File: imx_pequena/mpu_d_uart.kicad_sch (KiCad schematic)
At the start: 1 part, among them U1 MCIMX6Z0DVM09AB

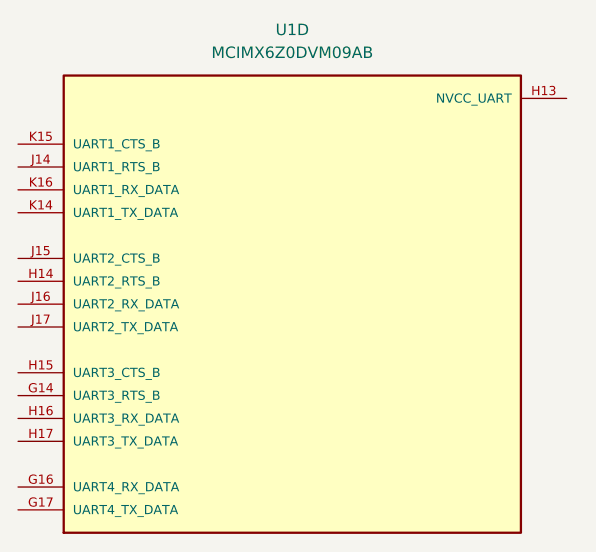
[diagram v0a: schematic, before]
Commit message: SD card + pinot files
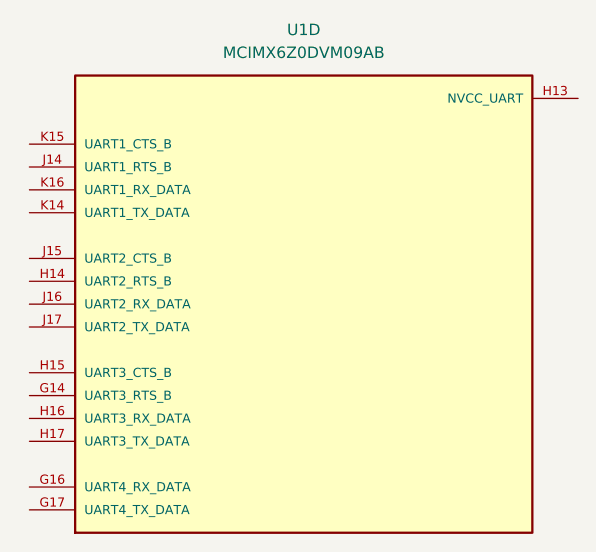
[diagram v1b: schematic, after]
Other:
- moved on the sheet: U1D
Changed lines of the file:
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@@
 (kicad_sch (version 20211123) (generator eeschema)
   (paper "A4")
-  (symbol (lib_id "MCIMX6Z0DVM09AB:MCIMX6Z0DVM09AB") (at 132.08 76.2 0) (unit 4)
+  (symbol (lib_id "MCIMX6Z0DVM09AB:MCIMX6Z0DVM09AB") (at 133.35 76.2 0) (unit 4)
     (in_bom yes) (on_board yes) (fields_autoplaced)
-    (property "Reference" "U1" (id 0) (at 132.08 45.72 0))
-    (property "Value" "MCIMX6Z0DVM09AB" (id 1) (at 132.08 48.26 0))
-    (property "Footprint" "mb_nxp_mcu_mpu:BGA289C80P17X17_1400X1400X132" (id 2) (at 132.08 76.2 0)
+    (property "Reference" "U1" (id 0) (at 133.35 45.72 0))
+    (property "Value" "MCIMX6Z0DVM09AB" (id 1) (at 133.35 48.26 0))
+    (property "Footprint" "mb_nxp_mcu_mpu:BGA289C80P17X17_1400X1400X132" (id 2) (at 133.35 76.2 0)
       (effects (font (size 1.27 1.27)) (justify bottom) hide)
     )
-    (property "Datasheet" "" (id 3) (at 132.08 76.2 0)
+    (property "Datasheet" "" (id 3) (at 133.35 76.2 0)
       (effects (font (size 1.27 1.27)) hide)
     )
-    (property "PARTREV" "0" (id 4) (at 132.08 76.2 0)
+    (property "PARTREV" "0" (id 4) (at 133.35 76.2 0)
       (effects (font (size 1.27 1.27)) (justify bottom) hide)
     )
-    (property "STANDARD" "IPC 7351B" (id 5) (at 132.08 76.2 0)
+    (property "STANDARD" "IPC 7351B" (id 5) (at 133.35 76.2 0)
       (effects (font (size 1.27 1.27)) (justify bottom) hide)
     )
-    (property "SNAPEDA_PN" "MCIMX6Z0DVM09AB" (id 6) (at 132.08 76.2 0)
+    (property "SNAPEDA_PN" "MCIMX6Z0DVM09AB" (id 6) (at 133.35 76.2 0)
       (effects (font (size 1.27 1.27)) (justify bottom) hide)
     )
-    (property "MAXIMUM_PACKAGE_HEIGHT" "1.32mm" (id 7) (at 132.08 76.2 0)
+    (property "MAXIMUM_PACKAGE_HEIGHT" "1.32mm" (id 7) (at 133.35 76.2 0)
       (effects (font (size 1.27 1.27)) (justify bottom) hide)
     )
-    (property "MANUFACTURER" "NXP" (id 8) (at 132.08 76.2 0)
+    (property "MANUFACTURER" "NXP" (id 8) (at 133.35 76.2 0)
       (effects (font (size 1.27 1.27)) (justify bottom) hide)
     )

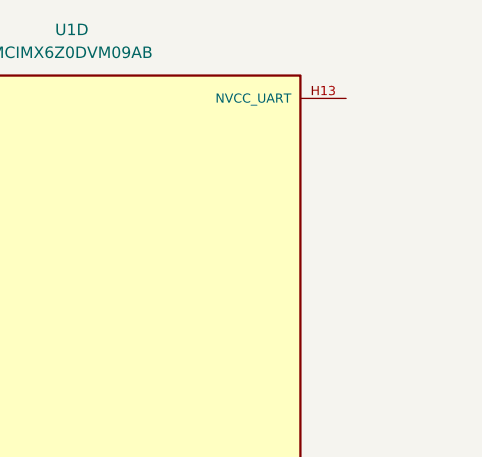
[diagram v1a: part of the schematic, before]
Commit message: Power Update
Added 3v3 and 1.35V switchers
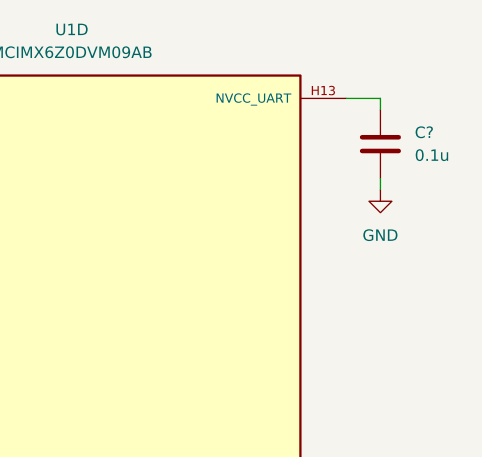
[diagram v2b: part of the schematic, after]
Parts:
- added C?: 0.1u, symbol Device:C
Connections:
- net at U1.H13 (NVCC_UART): now also C?.1
- new net GND: C?.2
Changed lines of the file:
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@@
 (kicad_sch (version 20211123) (generator eeschema)
   (paper "A4")
+  (wire (pts (xy 167.64 53.34) (xy 167.64 54.61))
+    (stroke (width 0) (type default) (color 0 0 0 0))
+  )
+  (wire (pts (xy 163.83 53.34) (xy 167.64 53.34))
+    (stroke (width 0) (type default) (color 0 0 0 0))
+  )
+  (wire (pts (xy 167.64 62.23) (xy 167.64 63.5))
+    (stroke (width 0) (type default) (color 0 0 0 0))
+  )
+  (symbol (lib_id "Device:C") (at 167.64 58.42 0) (unit 1)
+    (in_bom yes) (on_board yes) (fields_autoplaced)
+    (property "Reference" "C?" (id 0) (at 171.45 57.1499 0)
+      (effects (font (size 1.27 1.27)) (justify left))
+    )
+    (property "Value" "0.1u" (id 1) (at 171.45 59.6899 0)
+      (effects (font (size 1.27 1.27)) (justify left))
+    )
+    (property "Footprint" "" (id 2) (at 168.6052 62.23 0)
+      (effects (font (size 1.27 1.27)) hide)
+    )
+    (property "Datasheet" "~" (id 3) (at 167.64 58.42 0)
+      (effects (font (size 1.27 1.27)) hide)
+    )
+    (pin "1")
+    (pin "2")
+  )
+  (symbol (lib_id "power:GND") (at 167.64 63.5 0) (unit 1)
+    (in_bom yes) (on_board yes) (fields_autoplaced)
+    (property "Reference" "#PWR?" (id 0) (at 167.64 69.85 0)
+      (effects (font (size 1.27 1.27)) hide)
+    )
+    (property "Value" "GND" (id 1) (at 167.64 68.58 0))
+    (property "Footprint" "" (id 2) (at 167.64 63.5 0)
+      (effects (font (size 1.27 1.27)) hide)
+    )
+    (property "Datasheet" "" (id 3) (at 167.64 63.5 0)
+      (effects (font (size 1.27 1.27)) hide)
+    )
+    (pin "1")
+  )
   (symbol (lib_id "MCIMX6Z0DVM09AB:MCIMX6Z0DVM09AB") (at 133.35 76.2 0) (unit 4)
     (in_bom yes) (on_board yes) (fields_autoplaced)

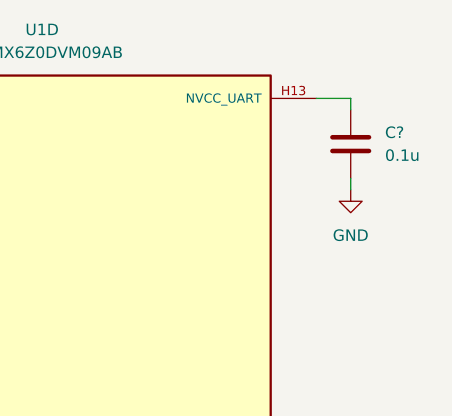
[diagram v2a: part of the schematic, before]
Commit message: Updated config
Updated config file and some pins
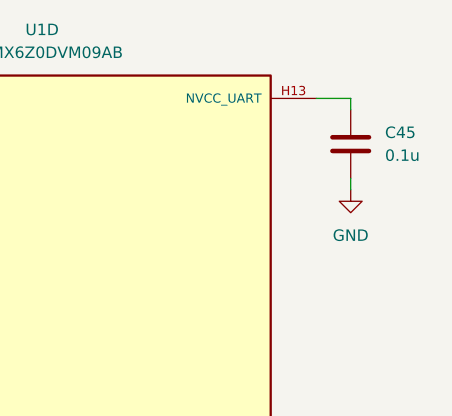
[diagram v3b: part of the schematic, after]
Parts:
- gave numbers to parts that had none: 1
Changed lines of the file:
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@@
   (symbol (lib_id "Device:C") (at 167.64 58.42 0) (unit 1)
     (in_bom yes) (on_board yes) (fields_autoplaced)
-    (property "Reference" "C?" (id 0) (at 171.45 57.1499 0)
+    (property "Reference" "C45" (id 0) (at 171.45 57.1499 0)
       (effects (font (size 1.27 1.27)) (justify left))
     )
@@
   (symbol (lib_id "power:GND") (at 167.64 63.5 0) (unit 1)
     (in_bom yes) (on_board yes) (fields_autoplaced)
-    (property "Reference" "#PWR?" (id 0) (at 167.64 69.85 0)
+    (property "Reference" "#PWR0131" (id 0) (at 167.64 69.85 0)
       (effects (font (size 1.27 1.27)) hide)
     )

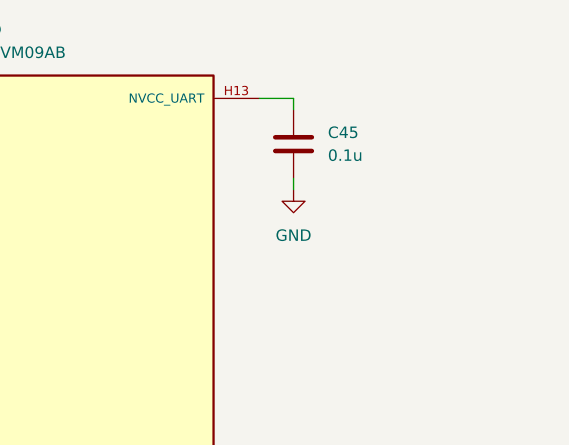
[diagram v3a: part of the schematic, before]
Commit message: Cleaned up NVCC pins
Added 3v3 connections + decoupling caps to NVcc pins
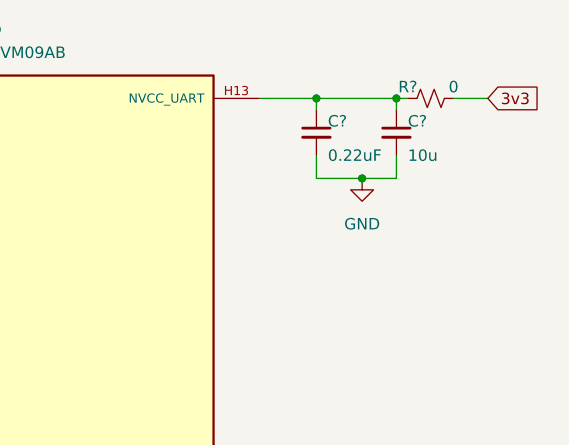
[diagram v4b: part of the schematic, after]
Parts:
- removed C45: 0.1u, symbol Device:C
- added C?: 10u, symbol Device:C_Small
- added C?: 0.22uF, symbol Device:C_Small
- added R?: 0, symbol Device:R_Small_US
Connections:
- net GND: now also C?.2, C?.2
- net at U1.H13 (NVCC_UART): now also C?.1, C?.1, R?.1
- new net 3v3: R?.2
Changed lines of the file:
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@@
 (kicad_sch (version 20211123) (generator eeschema)
   (paper "A4")
-  (wire (pts (xy 167.64 53.34) (xy 167.64 54.61))
+  (junction (at 175.26 62.23) (diameter 0) (color 0 0 0 0)
+  )
+  (junction (at 179.07 53.34) (diameter 0) (color 0 0 0 0)
+  )
+  (junction (at 170.18 53.34) (diameter 0) (color 0 0 0 0)
+  )
+  (wire (pts (xy 175.26 62.23) (xy 179.07 62.23))
     (stroke (width 0) (type default) (color 0 0 0 0))
   )
-  (wire (pts (xy 163.83 53.34) (xy 167.64 53.34))
+  (wire (pts (xy 170.18 53.34) (xy 179.07 53.34))
     (stroke (width 0) (type default) (color 0 0 0 0))
   )
-  (wire (pts (xy 167.64 62.23) (xy 167.64 63.5))
+  (wire (pts (xy 179.07 53.34) (xy 180.34 53.34))
     (stroke (width 0) (type default) (color 0 0 0 0))
   )
-  (symbol (lib_id "Device:C") (at 167.64 58.42 0) (unit 1)
+  (wire (pts (xy 170.18 59.69) (xy 170.18 62.23))
+    (stroke (width 0) (type default) (color 0 0 0 0))
+  )
+  (wire (pts (xy 185.42 53.34) (xy 189.23 53.34))
+    (stroke (width 0) (type default) (color 0 0 0 0))
+  )
+  (wire (pts (xy 170.18 53.34) (xy 170.18 54.61))
+    (stroke (width 0) (type default) (color 0 0 0 0))
+  )
+  (wire (pts (xy 163.83 53.34) (xy 170.18 53.34))
+    (stroke (width 0) (type default) (color 0 0 0 0))
+  )
+  (wire (pts (xy 179.07 59.69) (xy 179.07 62.23))
+    (stroke (width 0) (type default) (color 0 0 0 0))
+  )
+  (wire (pts (xy 179.07 53.34) (xy 179.07 54.61))
+    (stroke (width 0) (type default) (color 0 0 0 0))
+  )
+  (wire (pts (xy 170.18 62.23) (xy 175.26 62.23))
+    (stroke (width 0) (type default) (color 0 0 0 0))
+  )
+  (global_label "3v3" (shape input) (at 189.23 53.34 0) (fields_autoplaced)
+    (effects (font (size 1.27 1.27)) (justify left))
+    (property "Intersheet References" "${INTERSHEET_REFS}" (id 0) (at 195.0298 53.2606 0)
+      (effects (font (size 1.27 1.27)) (justify left) hide)
+    )
+  )
+  (symbol (lib_id "power:GND") (at 175.26 62.23 0) (unit 1)
     (in_bom yes) (on_board yes) (fields_autoplaced)
-    (property "Reference" "C45" (id 0) (at 171.45 57.1499 0)
-      (effects (font (size 1.27 1.27)) (justify left))
-    )
-    (property "Value" "0.1u" (id 1) (at 171.45 59.6899 0)
-      (effects (font (size 1.27 1.27)) (justify left))
-    )
-    (property "Footprint" "" (id 2) (at 168.6052 62.23 0)
+    (property "Reference" "#PWR?" (id 0) (at 175.26 68.58 0)
       (effects (font (size 1.27 1.27)) hide)
     )
-    (property "Datasheet" "~" (id 3) (at 167.64 58.42 0)
+    (property "Value" "GND" (id 1) (at 175.26 67.31 0))
+    (property "Footprint" "" (id 2) (at 175.26 62.23 0)
+      (effects (font (size 1.27 1.27)) hide)
+    )
+    (property "Datasheet" "" (id 3) (at 175.26 62.23 0)
+      (effects (font (size 1.27 1.27)) hide)
+    )
+    (pin "1")
+  )
+  (symbol (lib_id "Device:R_Small_US") (at 182.88 53.34 90) (unit 1)
+    (in_bom yes) (on_board yes)
+    (property "Reference" "R?" (id 0) (at 180.34 52.07 90))
+    (property "Value" "0" (id 1) (at 185.42 52.07 90))
+    (property "Footprint" "" (id 2) (at 182.88 53.34 0)
+      (effects (font (size 1.27 1.27)) hide)
+    )
+    (property "Datasheet" "~" (id 3) (at 182.88 53.34 0)
       (effects (font (size 1.27 1.27)) hide)
     )
@@
     (pin "2")
   )
-  (symbol (lib_id "power:GND") (at 167.64 63.5 0) (unit 1)
-    (in_bom yes) (on_board yes) (fields_autoplaced)
-    (property "Reference" "#PWR0131" (id 0) (at 167.64 69.85 0)
+  (symbol (lib_id "Device:C_Small") (at 179.07 57.15 0) (unit 1)
+    (in_bom yes) (on_board yes)
+    (property "Reference" "C?" (id 0) (at 180.34 55.88 0)
+      (effects (font (size 1.27 1.27)) (justify left))
+    )
+    (property "Value" "10u" (id 1) (at 180.34 59.69 0)
+      (effects (font (size 1.27 1.27)) (justify left))
+    )
+    (property "Footprint" "" (id 2) (at 179.07 57.15 0)
       (effects (font (size 1.27 1.27)) hide)
     )
-    (property "Value" "GND" (id 1) (at 167.64 68.58 0))
-    (property "Footprint" "" (id 2) (at 167.64 63.5 0)
-      (effects (font (size 1.27 1.27)) hide)
-    )
-    (property "Datasheet" "" (id 3) (at 167.64 63.5 0)
+    (property "Datasheet" "~" (id 3) (at 179.07 57.15 0)
       (effects (font (size 1.27 1.27)) hide)
     )
     (pin "1")
+    (pin "2")
+  )
+  (symbol (lib_id "Device:C_Small") (at 170.18 57.15 0) (unit 1)
+    (in_bom yes) (on_board yes)
+    (property "Reference" "C?" (id 0) (at 171.45 55.88 0)
+      (effects (font (size 1.27 1.27)) (justify left))
+    )
+    (property "Value" "0.22uF" (id 1) (at 171.45 59.69 0)
+      (effects (font (size 1.27 1.27)) (justify left))
+    )
+    (property "Footprint" "" (id 2) (at 170.18 57.15 0)
+      (effects (font (size 1.27 1.27)) hide)
+    )
+    (property "Datasheet" "~" (id 3) (at 170.18 57.15 0)
+      (effects (font (size 1.27 1.27)) hide)
+    )
+    (pin "1")
+    (pin "2")
   )
   (symbol (lib_id "MCIMX6Z0DVM09AB:MCIMX6Z0DVM09AB") (at 133.35 76.2 0) (unit 4)
